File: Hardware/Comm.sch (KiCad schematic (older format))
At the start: 14 parts, among them P201 CONN_01X06, P202 CONN_01X04, P203 CONN_01X04, P204 CONN_01X03, SW201 FSM2JSMAA-ND

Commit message: Rename project files to remove the space between 'Central' & 'Command' for the XSL processing of the BOM
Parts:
- C201: value C -> .1
- R201, R202, R204: value R -> 10K
- SW201: value FSM2JSMAA-ND -> PushButton; Link (none) -> http://www.digikey.com/product-detail/en/FSM2JSMAA/FSM2JSMA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; MPN (none) -> FSM2JSMAA
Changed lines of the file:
@@
 EESchema Schematic File Version 2
-LIBS:Central Command-rescue
 LIBS:power
 LIBS:device
@@
 LIBS:valves
 LIBS:stm32f030c8
-LIBS:Central Command-cache
+LIBS:CentralCommand-cache
 EELAYER 25 0
 EELAYER END
@@
 P 2650 4200
 F 0 "R201" V 2730 4200 50  0000 C CNN
-F 1 "R" V 2650 4200 50  0000 C CNN
+F 1 "10K" V 2650 4200 50  0000 C CNN
 F 2 "Resistors_SMD:R_0805" V 2580 4200 30  0001 C CNN
 F 3 "" H 2650 4200 30  0000 C CNN
@@
 P 2850 3550
 F 0 "R202" V 2930 3550 50  0000 C CNN
-F 1 "R" V 2850 3550 50  0000 C CNN
+F 1 "10K" V 2850 3550 50  0000 C CNN
 F 2 "Resistors_SMD:R_0805" V 2780 3550 30  0001 C CNN
 F 3 "" H 2850 3550 30  0000 C CNN
@@
 P 3750 4650
 F 0 "R204" V 3830 4650 50  0000 C CNN
-F 1 "R" V 3750 4650 50  0000 C CNN
+F 1 "10K" V 3750 4650 50  0000 C CNN
 F 2 "Resistors_SMD:R_0805" V 3680 4650 30  0001 C CNN
 F 3 "" H 3750 4650 30  0000 C CNN
@@
 P 5450 5550
 F 0 "C201" H 5475 5650 50  0000 L CNN
-F 1 "C" H 5475 5450 50  0000 L CNN
+F 1 ".1" H 5475 5450 50  0000 L CNN
 F 2 "Capacitors_SMD:C_0805" H 5488 5400 30  0001 C CNN
 F 3 "" H 5450 5550 60  0000 C CNN
@@
 P 5750 5750
 F 0 "SW201" H 5900 5860 50  0000 C CNN
-F 1 "FSM2JSMAA-ND" H 5750 5670 50  0000 C CNN
+F 1 "PushButton" H 5750 5670 50  0000 C CNN
 F 2 "CentralCommand:FSM2JSMAA-ND" H 5750 5750 60  0001 C CNN
-F 3 "http://www.digikey.com/product-detail/en/FSM2JSMAA/FSM2JSMAA-ND/2400228" H 5750 5750 60  0001 C CNN
+F 3 "" H 5750 5750 60  0001 C CNN
+F 4 "FSM2JSMAA" H 5750 5750 60  0001 C CNN "MPN"
+F 5 "http://www.digikey.com/product-detail/en/FSM2JSMAA/FSM2JSMAA-ND/2400228" H 5750 5750 60  0001 C CNN "Link"
 	1    5750 5750
 	0    1    1    0
@@
 	7450 5950 7450 6250
 $Comp
-L GND #PWR09
+L GND #PWR08
 U 1 1 5661772D
 P 7450 6250
-F 0 "#PWR09" H 7450 6000 50  0001 C CNN
+F 0 "#PWR08" H 7450 6000 50  0001 C CNN
 F 1 "GND" H 7450 6100 50  0000 C CNN
 F 2 "" H 7450 6250 60  0000 C CNN

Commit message: - Added Farnell and digi-key supplier numbers to most past. Still need todo crystal, switch and micro inductor. - updated the HTML BOM and CSV
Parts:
- C201: value .1 -> .1U; Farnell (none) -> 2496944; MPN (none) -> 0805B104K500CT
- P201: Farnell (none) -> 1022255; MPN (none) -> M20-9990646
- P202, P203: Farnell (none) -> 1022251; MPN (none) -> M20-9990446
- P204: Farnell (none) -> 1022249; MPN (none) -> M20-9990346
- R201, R202, R204: Farnell (none) -> 2447553; MPN (none) -> MCWR08X1002FTL
- R203, R206, R207, R208, R209: Farnell (none) -> 9333681; MPN (none) -> MC01W08050R
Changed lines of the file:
@@
 F 2 "CentralCommand:Grove-2mm" H 5400 1350 60  0001 C CNN
 F 3 "" H 5400 1350 60  0000 C CNN
+F 4 "1022251" H 5400 1350 60  0001 C CNN "Farnell"
+F 5 "M20-9990446" H 5400 1350 60  0001 C CNN "MPN"
 	1    5400 1350
 	1    0    0    -1
@@
 F 2 "CentralCommand:Grove-2mm" H 5400 2550 60  0001 C CNN
 F 3 "" H 5400 2550 60  0000 C CNN
+F 4 "M20-9990446" H 5400 2550 60  0001 C CNN "MPN"
+F 5 "1022251" H 5400 2550 60  0001 C CNN "Farnell"
 	1    5400 2550
 	1    0    0    -1
@@
 F 2 "Pin_Headers:Pin_Header_Straight_1x06" H 3950 4050 60  0001 C CNN
 F 3 "" H 3950 4050 60  0000 C CNN
+F 4 "1022255" H 3950 4050 60  0001 C CNN "Farnell"
+F 5 "M20-9990646" H 3950 4050 60  0001 C CNN "MPN"
 	1    3950 4050
 	1    0    0    -1
@@
 F 2 "Resistors_SMD:R_0805" V 3580 3550 30  0001 C CNN
 F 3 "" H 3650 3550 30  0000 C CNN
+F 4 "9333681" V 3650 3550 60  0001 C CNN "Farnell"
+F 5 "MC01W08050R" V 3650 3550 60  0001 C CNN "MPN"
 	1    3650 3550
 	-1   0    0    -1
@@
 F 2 "Resistors_SMD:R_0805" V 2580 4200 30  0001 C CNN
 F 3 "" H 2650 4200 30  0000 C CNN
+F 4 "2447553" V 2650 4200 60  0001 C CNN "Farnell"
+F 5 "MCWR08X1002FTL" V 2650 4200 60  0001 C CNN "MPN"
 	1    2650 4200
 	-1   0    0    -1
@@
 F 2 "Resistors_SMD:R_0805" V 2780 3550 30  0001 C CNN
 F 3 "" H 2850 3550 30  0000 C CNN
+F 4 "2447553" V 2850 3550 60  0001 C CNN "Farnell"
+F 5 "MCWR08X1002FTL" V 2850 3550 60  0001 C CNN "MPN"
 	1    2850 3550
 	-1   0    0    -1
@@
 F 2 "Resistors_SMD:R_0805" V 3680 4650 30  0001 C CNN
 F 3 "" H 3750 4650 30  0000 C CNN
+F 4 "2447553" V 3750 4650 60  0001 C CNN "Farnell"
+F 5 "MCWR08X1002FTL" V 3750 4650 60  0001 C CNN "MPN"
 	1    3750 4650
 	-1   0    0    -1
@@
 P 5450 5550
 F 0 "C201" H 5475 5650 50  0000 L CNN
-F 1 ".1" H 5475 5450 50  0000 L CNN
+F 1 ".1U" H 5475 5450 50  0000 L CNN
 F 2 "Capacitors_SMD:C_0805" H 5488 5400 30  0001 C CNN
 F 3 "" H 5450 5550 60  0000 C CNN
+F 4 "2496944" H 5450 5550 60  0001 C CNN "Farnell"
+F 5 "0805B104K500CT" H 5450 5550 60  0001 C CNN "MPN"
 	1    5450 5550
 	1    0    0    -1
@@
 F 2 "Pin_Headers:Pin_Header_Straight_1x03" H 7800 5850 60  0001 C CNN
 F 3 "" H 7800 5850 60  0000 C CNN
+F 4 "1022249" H 7800 5850 60  0001 C CNN "Farnell"
+F 5 "M20-9990346" H 7800 5850 60  0001 C CNN "MPN"
 	1    7800 5850
 	1    0    0    -1
@@
 F 2 "Resistors_SMD:R_0805" V 4730 2050 30  0001 C CNN
 F 3 "" H 4800 2050 30  0000 C CNN
+F 4 "9333681" V 4800 2050 60  0001 C CNN "Farnell"
+F 5 "MC01W08050R" V 4800 2050 60  0001 C CNN "MPN"
 	1    4800 2050
 	1    0    0    -1
@@
 F 2 "Resistors_SMD:R_0805" V 4630 2050 30  0001 C CNN
 F 3 "" H 4700 2050 30  0000 C CNN
+F 4 "9333681" V 4700 2050 60  0001 C CNN "Farnell"
+F 5 "MC01W08050R" V 4700 2050 60  0001 C CNN "MPN"
 	1    4700 2050
 	1    0    0    -1
@@
 F 2 "Resistors_SMD:R_0805" V 4530 2050 30  0001 C CNN
 F 3 "" H 4600 2050 30  0000 C CNN
+F 4 "9333681" V 4600 2050 60  0001 C CNN "Farnell"
+F 5 "MC01W08050R" V 4600 2050 60  0001 C CNN "MPN"
 	1    4600 2050
 	1    0    0    -1
@@
 F 2 "Resistors_SMD:R_0805" V 4430 2050 30  0001 C CNN
 F 3 "" H 4500 2050 30  0000 C CNN
+F 4 "9333681" V 4500 2050 60  0001 C CNN "Farnell"
+F 5 "MC01W08050R" V 4500 2050 60  0001 C CNN "MPN"
 	1    4500 2050
 	1    0    0    -1

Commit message: Added the farnell code for the last few parts
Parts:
- SW201: Farnell (none) -> 2468760
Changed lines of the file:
@@
 F 4 "FSM2JSMAA" H 5750 5750 60  0001 C CNN "MPN"
 F 5 "http://www.digikey.com/product-detail/en/FSM2JSMAA/FSM2JSMAA-ND/2400228" H 5750 5750 60  0001 C CNN "Link"
+F 6 "2468760" H 5750 5750 60  0001 C CNN "Farnell"
 	1    5750 5750
 	0    1    1    0

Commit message: Fixed the seed studion connect farnell code. It now points to the 2mm version
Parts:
- P202, P203: value CONN_01X04 -> CONN_01X04_2mm; Farnell 1022251 -> 2289778; MPN M20-9990446 -> M22-2510405
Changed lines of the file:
@@
 P 5400 1350
 F 0 "P202" H 5400 1600 50  0000 C CNN
-F 1 "CONN_01X04" V 5500 1350 50  0000 C CNN
+F 1 "CONN_01X04_2mm" V 5500 1350 50  0000 C CNN
 F 2 "CentralCommand:Grove-2mm" H 5400 1350 60  0001 C CNN
 F 3 "" H 5400 1350 60  0000 C CNN
-F 4 "1022251" H 5400 1350 60  0001 C CNN "Farnell"
-F 5 "M20-9990446" H 5400 1350 60  0001 C CNN "MPN"
+F 4 "2289778" H 5400 1350 60  0001 C CNN "Farnell"
+F 5 "M22-2510405" H 5400 1350 60  0001 C CNN "MPN"
 	1    5400 1350
 	1    0    0    -1
@@
 P 5400 2550
 F 0 "P203" H 5400 2800 50  0000 C CNN
-F 1 "CONN_01X04" V 5500 2550 50  0000 C CNN
+F 1 "CONN_01X04_2mm" V 5500 2550 50  0000 C CNN
 F 2 "CentralCommand:Grove-2mm" H 5400 2550 60  0001 C CNN
 F 3 "" H 5400 2550 60  0000 C CNN
-F 4 "M20-9990446" H 5400 2550 60  0001 C CNN "MPN"
-F 5 "1022251" H 5400 2550 60  0001 C CNN "Farnell"
+F 4 "M22-2510405" H 5400 2550 60  0001 C CNN "MPN"
+F 5 "2289778" H 5400 2550 60  0001 C CNN "Farnell"
 	1    5400 2550
 	1    0    0    -1

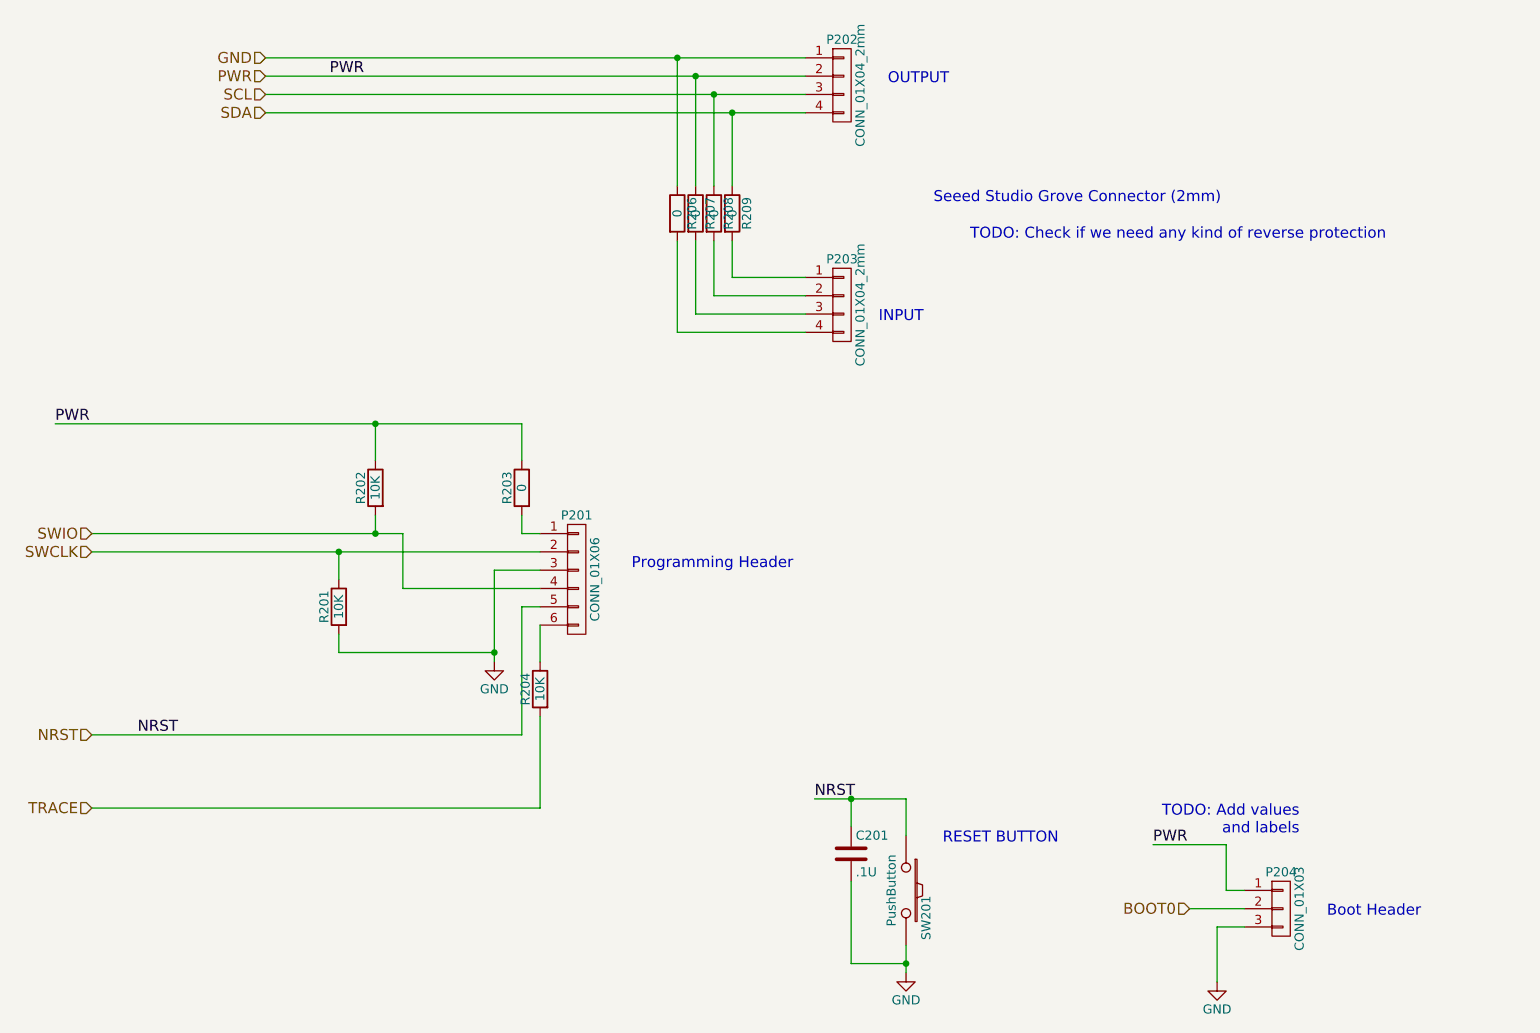
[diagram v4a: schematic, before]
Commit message: Changed the component values to hold MPNs for Macrofab processing
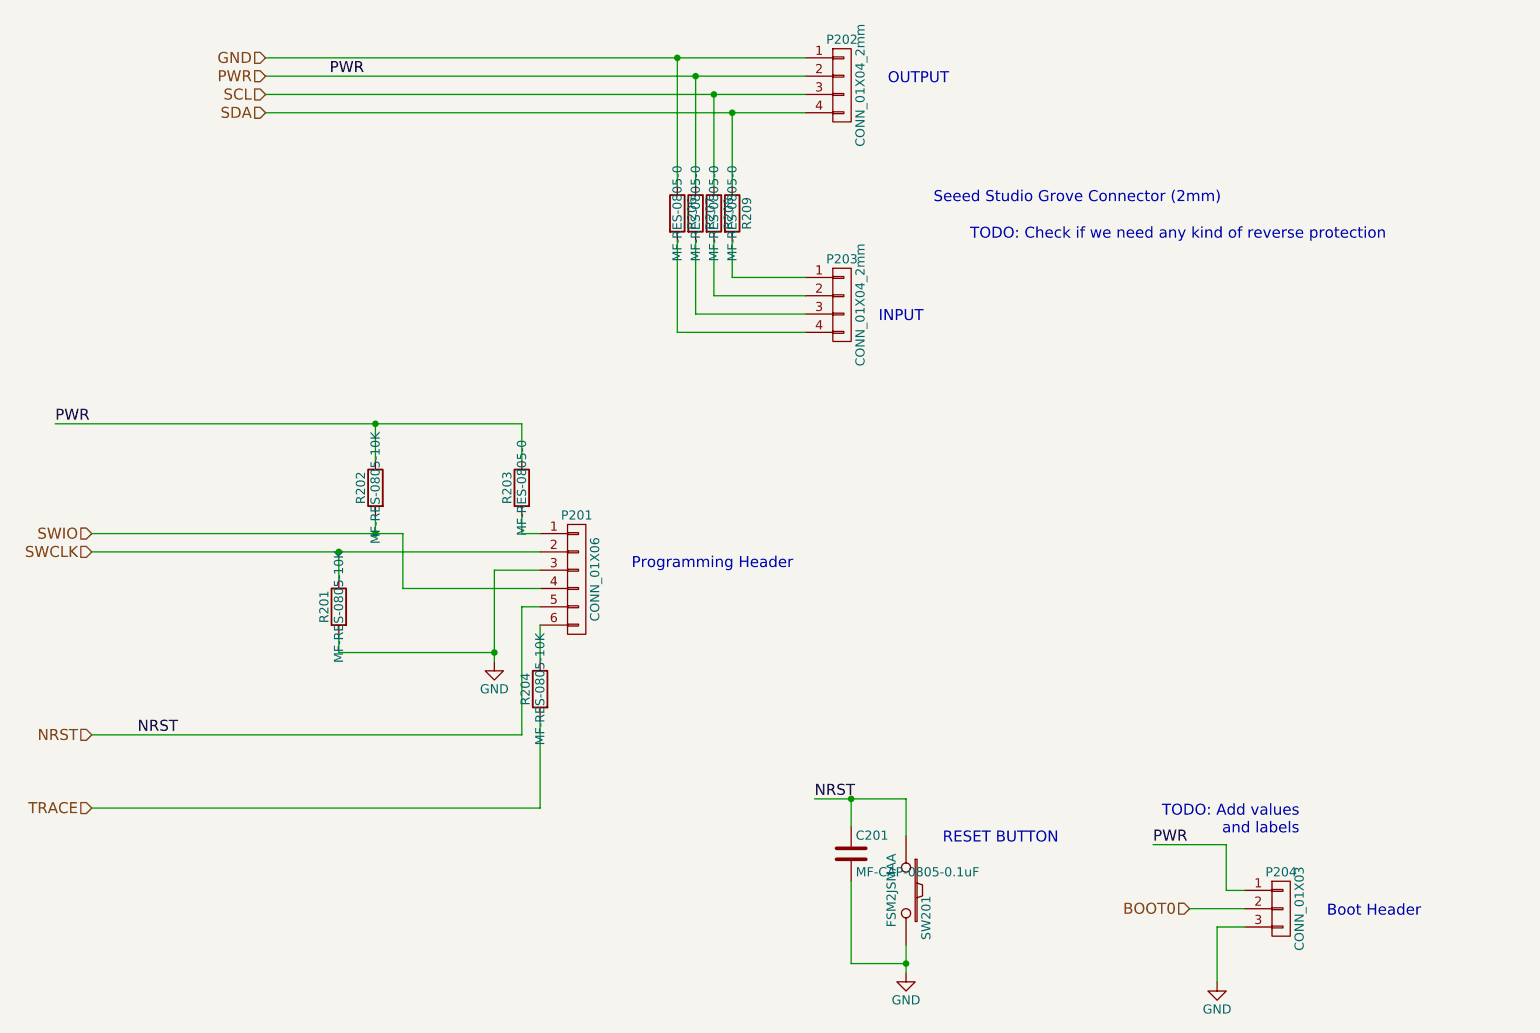
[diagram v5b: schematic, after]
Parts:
- C201: value .1U -> MF-CAP-0805-0.1uF
- R201, R202, R204: value 10K -> MF-RES-0805-10K
- R203, R206, R207, R208, R209: value 0 -> MF-RES-0805-0
- SW201: value PushButton -> FSM2JSMAA
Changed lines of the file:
@@
 P 3650 3550
 F 0 "R203" V 3730 3550 50  0000 C CNN
-F 1 "0" V 3650 3550 50  0000 C CNN
+F 1 "MF-RES-0805-0" V 3650 3550 50  0000 C CNN
 F 2 "Resistors_SMD:R_0805" V 3580 3550 30  0001 C CNN
 F 3 "" H 3650 3550 30  0000 C CNN
@@
 P 2650 4200
 F 0 "R201" V 2730 4200 50  0000 C CNN
-F 1 "10K" V 2650 4200 50  0000 C CNN
+F 1 "MF-RES-0805-10K" V 2650 4200 50  0000 C CNN
 F 2 "Resistors_SMD:R_0805" V 2580 4200 30  0001 C CNN
 F 3 "" H 2650 4200 30  0000 C CNN
@@
 P 2850 3550
 F 0 "R202" V 2930 3550 50  0000 C CNN
-F 1 "10K" V 2850 3550 50  0000 C CNN
+F 1 "MF-RES-0805-10K" V 2850 3550 50  0000 C CNN
 F 2 "Resistors_SMD:R_0805" V 2780 3550 30  0001 C CNN
 F 3 "" H 2850 3550 30  0000 C CNN
@@
 P 3750 4650
 F 0 "R204" V 3830 4650 50  0000 C CNN
-F 1 "10K" V 3750 4650 50  0000 C CNN
+F 1 "MF-RES-0805-10K" V 3750 4650 50  0000 C CNN
 F 2 "Resistors_SMD:R_0805" V 3680 4650 30  0001 C CNN
 F 3 "" H 3750 4650 30  0000 C CNN
@@
 P 5450 5550
 F 0 "C201" H 5475 5650 50  0000 L CNN
-F 1 ".1U" H 5475 5450 50  0000 L CNN
+F 1 "MF-CAP-0805-0.1uF" H 5475 5450 50  0000 L CNN
 F 2 "Capacitors_SMD:C_0805" H 5488 5400 30  0001 C CNN
 F 3 "" H 5450 5550 60  0000 C CNN
@@
 P 5750 5750
 F 0 "SW201" H 5900 5860 50  0000 C CNN
-F 1 "PushButton" H 5750 5670 50  0000 C CNN
+F 1 "FSM2JSMAA" H 5750 5670 50  0000 C CNN
 F 2 "CentralCommand:FSM2JSMAA-ND" H 5750 5750 60  0001 C CNN
 F 3 "" H 5750 5750 60  0001 C CNN
-F 4 "FSM2JSMAA" H 5750 5750 60  0001 C CNN "MPN"
-F 5 "http://www.digikey.com/product-detail/en/FSM2JSMAA/FSM2JSMAA-ND/2400228" H 5750 5750 60  0001 C CNN "Link"
+F 4 "http://www.digikey.com/product-detail/en/FSM2JSMAA/FSM2JSMAA-ND/2400228" H 5750 5750 60  0001 C CNN "Link"
+F 5 "FSM2JSMAA" H 5750 5750 60  0001 C CNN "MPN"
 F 6 "2468760" H 5750 5750 60  0001 C CNN "Farnell"
 	1    5750 5750
@@
 P 4800 2050
 F 0 "R209" V 4880 2050 50  0000 C CNN
-F 1 "0" V 4800 2050 50  0000 C CNN
+F 1 "MF-RES-0805-0" V 4800 2050 50  0000 C CNN
 F 2 "Resistors_SMD:R_0805" V 4730 2050 30  0001 C CNN
 F 3 "" H 4800 2050 30  0000 C CNN
@@
 P 4700 2050
 F 0 "R208" V 4780 2050 50  0000 C CNN
-F 1 "0" V 4700 2050 50  0000 C CNN
+F 1 "MF-RES-0805-0" V 4700 2050 50  0000 C CNN
 F 2 "Resistors_SMD:R_0805" V 4630 2050 30  0001 C CNN
 F 3 "" H 4700 2050 30  0000 C CNN
@@
 P 4600 2050
 F 0 "R207" V 4680 2050 50  0000 C CNN
-F 1 "0" V 4600 2050 50  0000 C CNN
+F 1 "MF-RES-0805-0" V 4600 2050 50  0000 C CNN
 F 2 "Resistors_SMD:R_0805" V 4530 2050 30  0001 C CNN
 F 3 "" H 4600 2050 30  0000 C CNN
@@
 P 4500 2050
 F 0 "R206" V 4580 2050 50  0000 C CNN
-F 1 "0" V 4500 2050 50  0000 C CNN
+F 1 "MF-RES-0805-0" V 4500 2050 50  0000 C CNN
 F 2 "Resistors_SMD:R_0805" V 4430 2050 30  0001 C CNN
 F 3 "" H 4500 2050 30  0000 C CNN
